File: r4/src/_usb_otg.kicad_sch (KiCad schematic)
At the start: 7 parts, among them J15 10118194, Q4 NX3008NBKW, U15 FSUSB42MX, U16 ESD7004

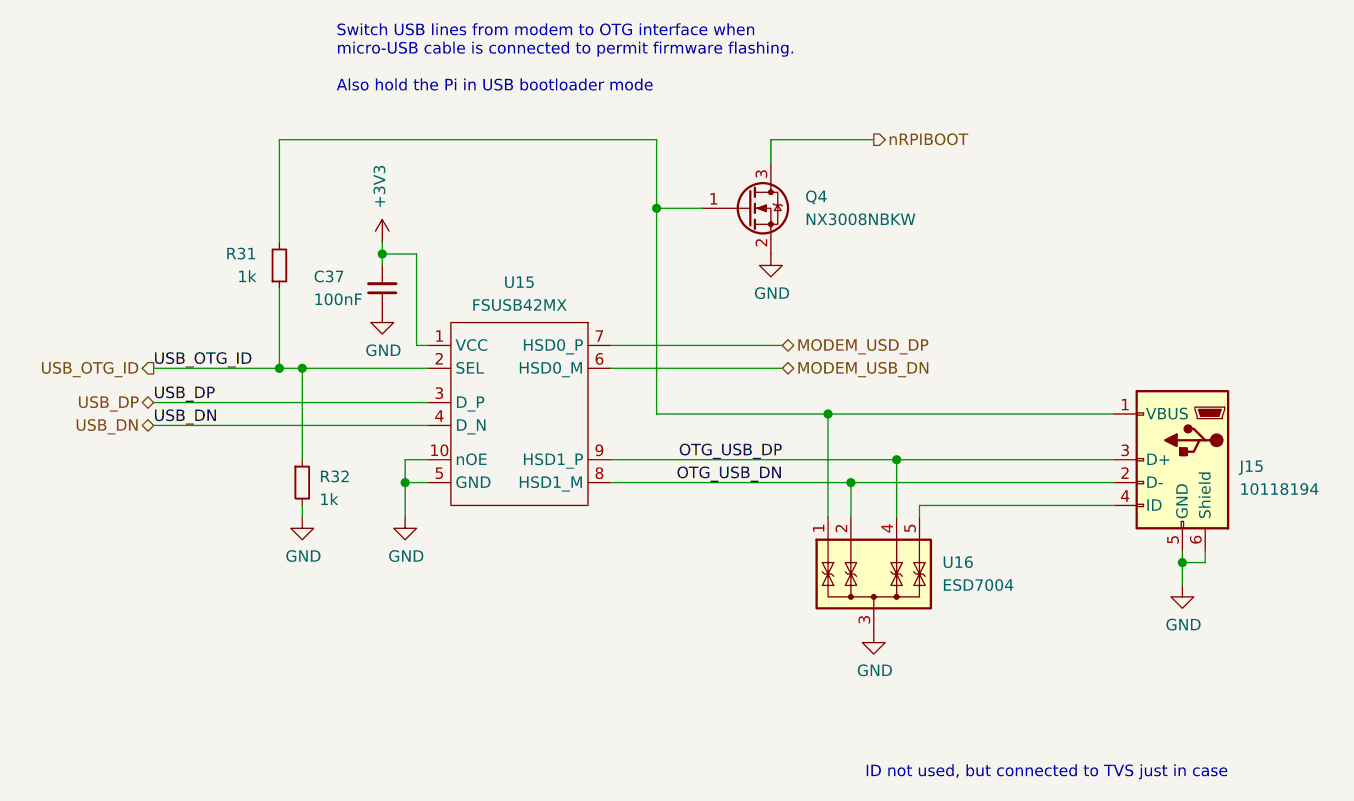
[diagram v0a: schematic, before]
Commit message: Update files to Kicad 6 format
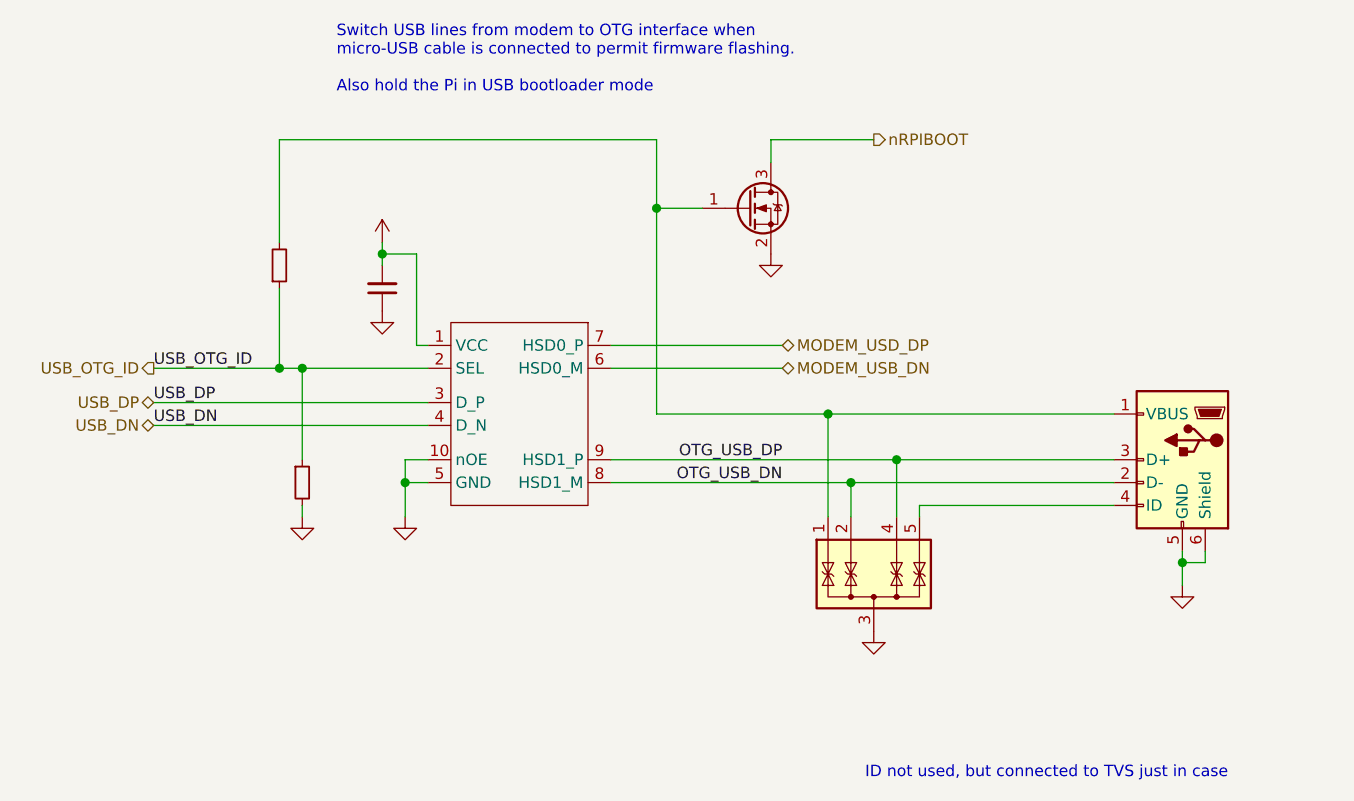
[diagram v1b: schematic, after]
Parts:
- ?: renamed from J15; value 10118194 -> (none); footprint Connector_USB:USB_Micro-B_Amphenol_10118194_Horizontal -> (none)
- ?: renamed from U16; value ESD7004 -> (none); footprint jeffmakes-footprints:USON-10_2.5x1.0mm_P0.5mm -> (none)
- ?: renamed from U15; value FSUSB42MX -> (none); footprint Package_SO:MSOP-10_3x3mm_P0.5mm -> (none)
- ?: renamed from C37; value 100nF -> (none); footprint Capacitor_SMD:C_0603_1608Metric -> (none)
- ?: renamed from R32; value 1k -> (none); footprint Resistor_SMD:R_0603_1608Metric -> (none)
- ?: renamed from R31; value 1k -> (none); footprint Resistor_SMD:R_0603_1608Metric -> (none)
- ?: renamed from Q4; value NX3008NBKW -> (none); footprint Package_TO_SOT_SMD:SOT-323_SC-70 -> (none)

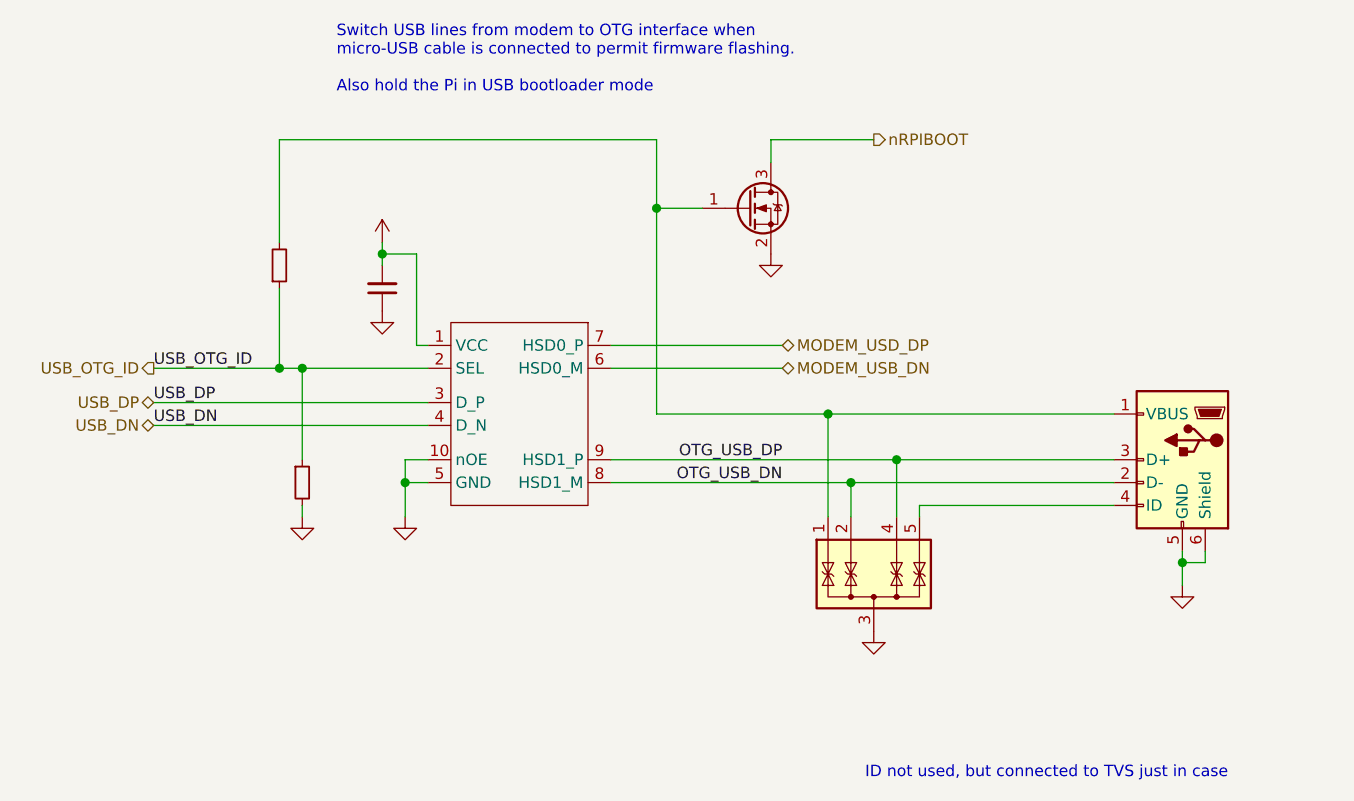
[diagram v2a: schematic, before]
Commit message: Add netclass definitions and assign nets. Define DRC rules to each class. Resize all vias and nets (with a few exceptions for very wide power tracks) to follow the netclass rules. Increase area for GNDA domain. Re-route SIM data bus around edge of GNDA domain
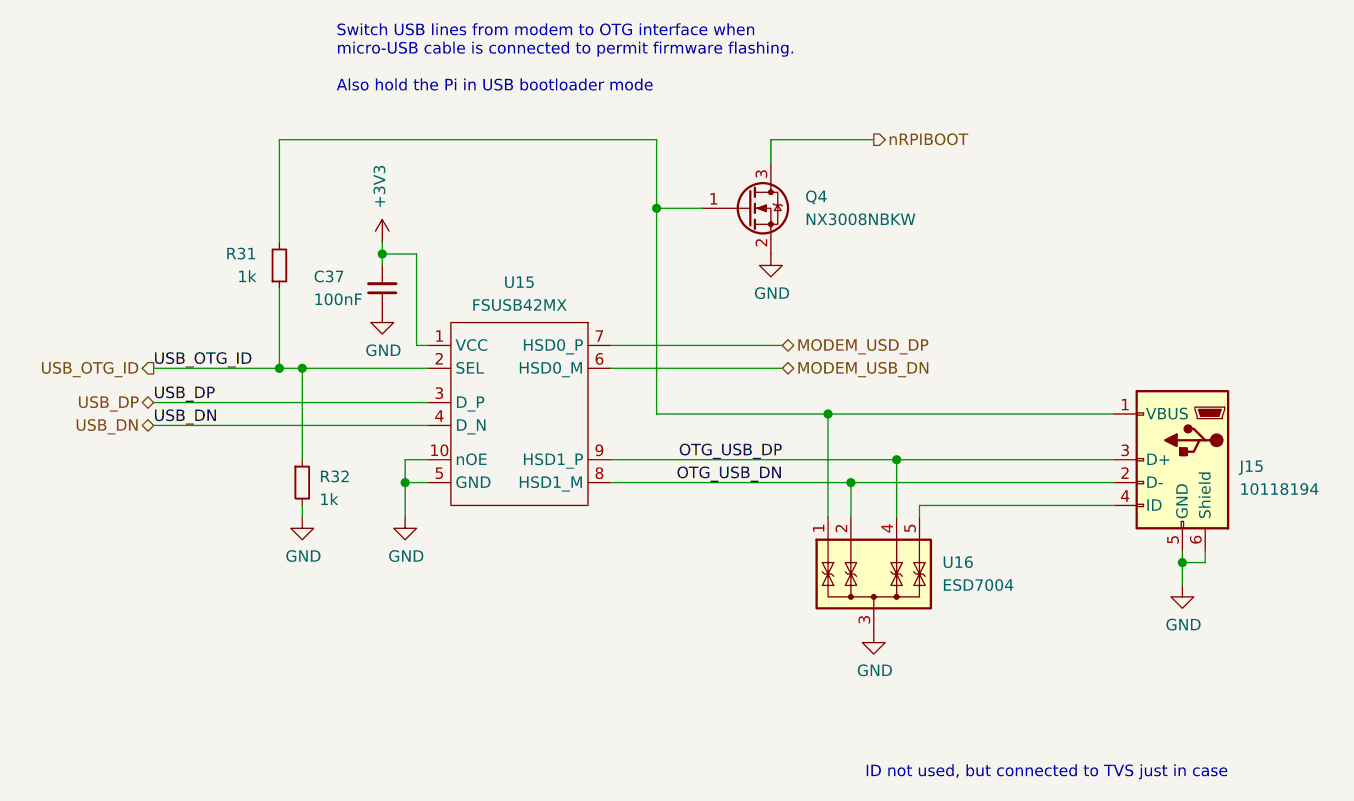
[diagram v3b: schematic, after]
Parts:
- C37: renamed from ?; value (none) -> 100nF; footprint (none) -> Capacitor_SMD:C_0603_1608Metric
- J15: renamed from ?; value (none) -> 10118194; footprint (none) -> Connector_USB:USB_Micro-B_Amphenol_10118194_Horizontal
- Q4: renamed from ?; value (none) -> NX3008NBKW; footprint (none) -> Package_TO_SOT_SMD:SOT-323_SC-70
- R31, R32: renamed from ?; value (none) -> 1k; footprint (none) -> Resistor_SMD:R_0603_1608Metric
- U15: renamed from ?; value (none) -> FSUSB42MX; footprint (none) -> Package_SO:MSOP-10_3x3mm_P0.5mm
- U16: renamed from ?; value (none) -> ESD7004; footprint (none) -> Package_SON:USON-10_2.5x1.0mm_P0.5mm

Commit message: Update TVS packs with pass-through routing
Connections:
- net GND: now also U16.8
- net OTG_USB_DN: now also U16.9
- net OTG_USB_DP: now also U16.7
- net at J15.1 (VBUS), Q4.1 (G), R31.2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: now also U16.10
- net at J15.4 (ID), U16.5 (IO4): now also U16.6
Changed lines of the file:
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@@
     (pin "3")
     (pin "1")
+    (pin "10")
     (pin "2")
     (pin "4")
     (pin "5")
+    (pin "6")
+    (pin "7")
+    (pin "8")
+    (pin "9")
     (instances
       (project "bugg-main-r4"

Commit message: Change some passive values and packages to get rid of some BOM lines
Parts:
- R31, R32: footprint Resistor_SMD:R_0603_1608Metric -> Resistor_SMD:R_0402_1005Metric
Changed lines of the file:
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@@
       (effects (font (size 1.27 1.27)) (justify left))
     )
-    (property "Footprint" "Resistor_SMD:R_0603_1608Metric" (at 109.22 109.22 0)
+    (property "Footprint" "Resistor_SMD:R_0402_1005Metric" (at 109.22 109.22 0)
       (effects (font (size 1.27 1.27)) hide)
     )
@@
       (project "bugg-main-r4"
         (path "/e3eb514f-6ce4-4abe-ba20-f82f0015628f/7086fb34-03e0-4978-93d2-ceae572d34d4"
-          (reference "R32") (unit 1) (value "1k") (footprint "Resistor_SMD:R_0603_1608Metric")
+          (reference "R32") (unit 1) (value "1k") (footprint "Resistor_SMD:R_0402_1005Metric")
         )
       )
@@
       (effects (font (size 1.27 1.27)) (justify right))
     )
-    (property "Footprint" "Resistor_SMD:R_0603_1608Metric" (at 106.68 85.09 0)
+    (property "Footprint" "Resistor_SMD:R_0402_1005Metric" (at 106.68 85.09 0)
       (effects (font (size 1.27 1.27)) hide)
     )
@@
       (project "bugg-main-r4"
         (path "/e3eb514f-6ce4-4abe-ba20-f82f0015628f/7086fb34-03e0-4978-93d2-ceae572d34d4"
-          (reference "R31") (unit 1) (value "1k") (footprint "Resistor_SMD:R_0603_1608Metric")
+          (reference "R31") (unit 1) (value "1k") (footprint "Resistor_SMD:R_0402_1005Metric")
         )
       )
